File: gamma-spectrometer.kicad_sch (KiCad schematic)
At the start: 48 parts, among them U1 Pico 2, U11 LM4040AIM3, U2 MAX1422ECM+D, U3 TLV3201AIDBVR, U4 MAX5026EUT_T, U6 MCP41050-I_SN, U7 MCP41050-I_SN

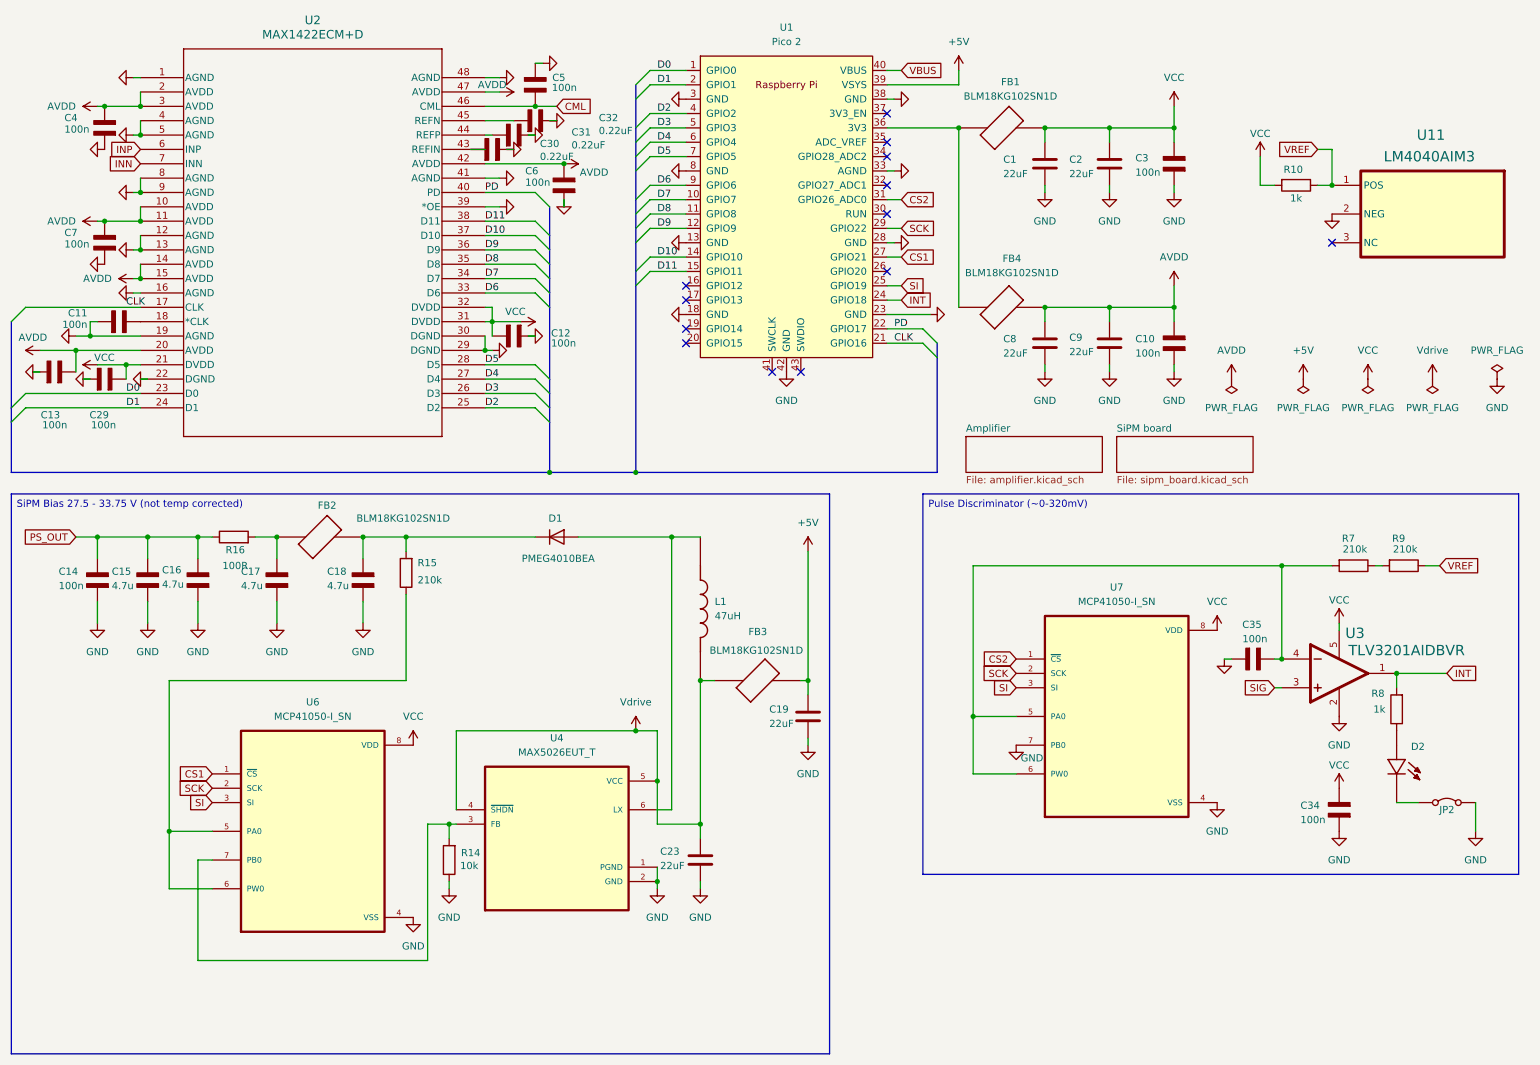
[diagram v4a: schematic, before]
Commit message: Modular SiPM board
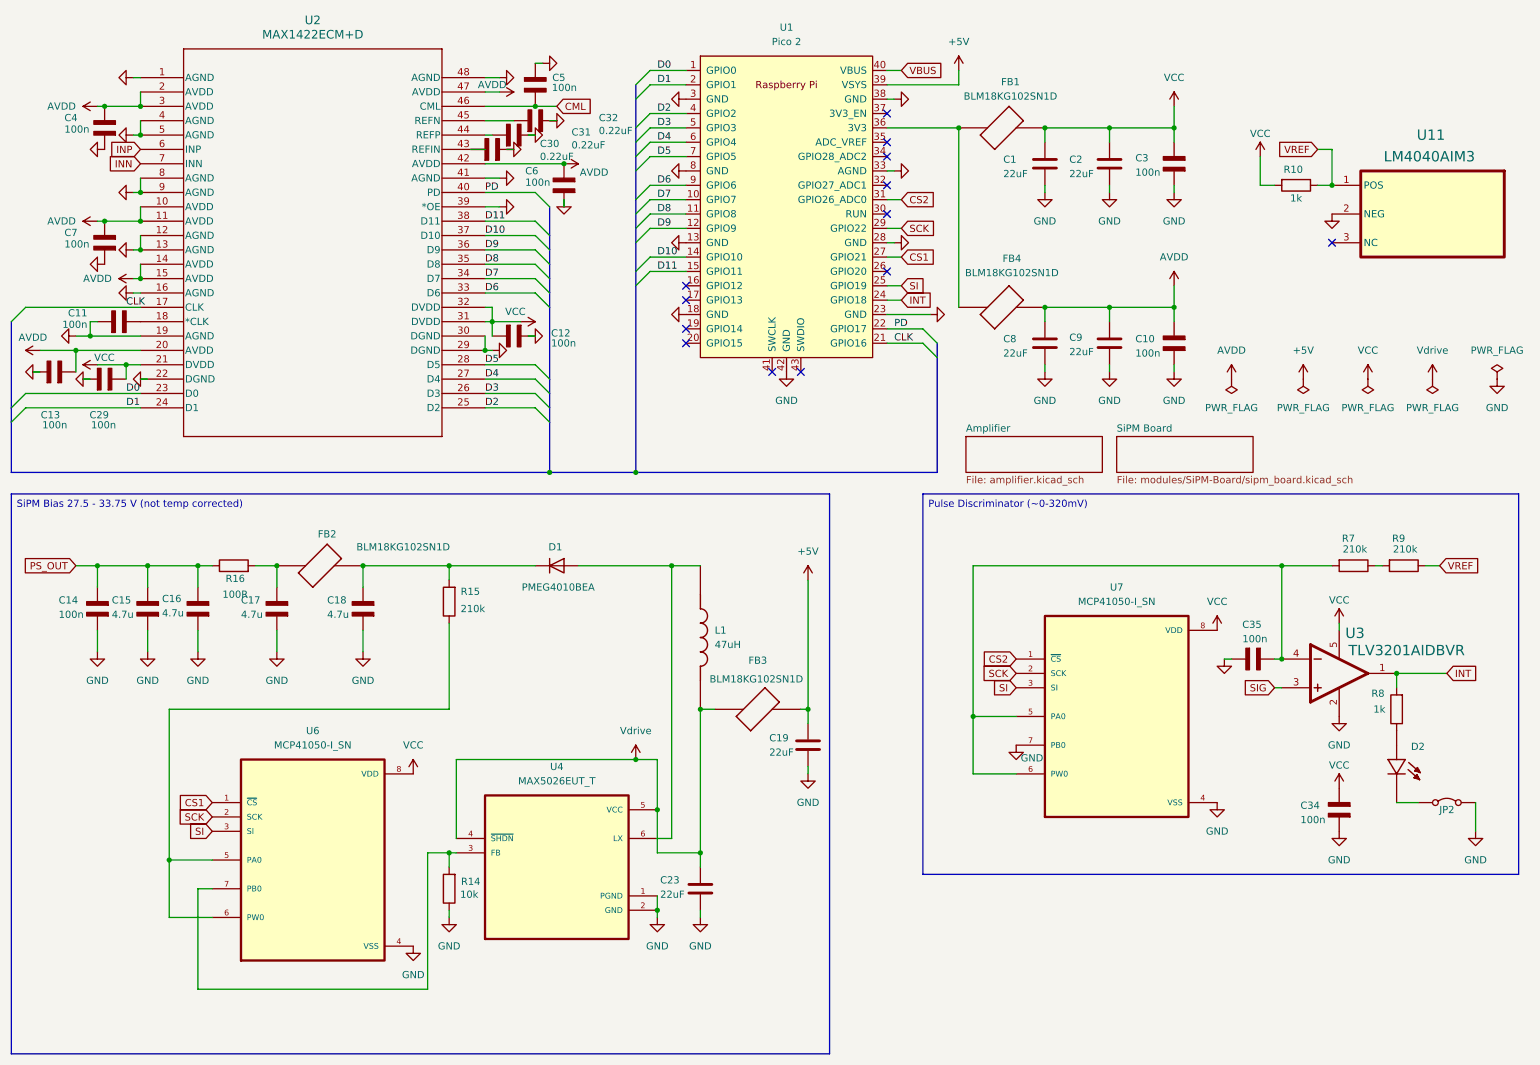
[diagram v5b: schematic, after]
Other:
- sheet SiPM board renamed SiPM Board
- sheet SiPM Board: file sipm_board.kicad_sch -> modules/SiPM-Board/sipm_board.kicad_sch
- moved on the sheet: C14, C15, C16, C17, C18, C19, C23, D1, FB2, FB3, L1, R14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
